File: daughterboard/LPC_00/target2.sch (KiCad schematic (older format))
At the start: 16 parts, among them U2 LPC55S69JBD64K

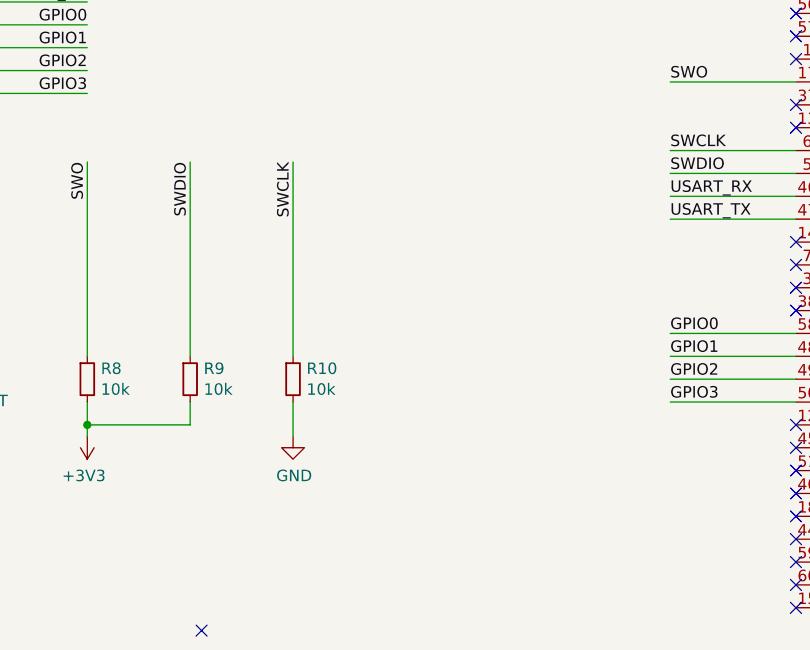
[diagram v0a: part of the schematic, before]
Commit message: ERC on daughterboards
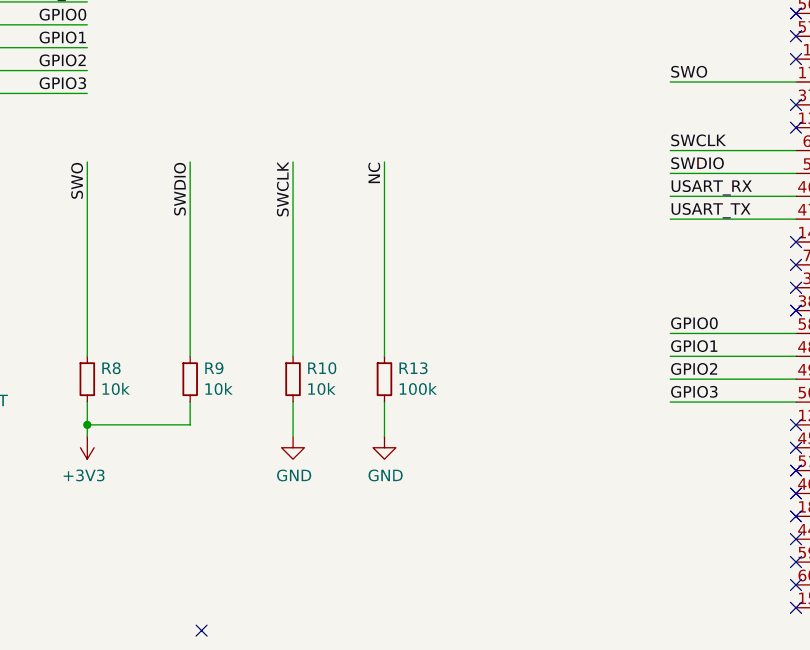
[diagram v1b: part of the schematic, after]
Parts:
- added R13: 100k, symbol Device:R_Small
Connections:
- net GND: now also R13.2
- net TDI|NC_2: now also R13.1
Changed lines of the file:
@@
 	8900 2200 8400 2200
-Wire Wire Line
-	7250 2150 7850 2150
 Wire Wire Line
 	7850 2150 7850 2500
@@
 NoConn ~ 7250 3100
 NoConn ~ 2700 5450
+Text Label 3500 3400 3    50   ~ 0
+NC
+$Comp
+L Device:R_Small R13
+U 1 1 618FD562
+P 3500 4350
+F 0 "R13" H 3559 4396 50  0000 L CNN
+F 1 "100k" H 3559 4305 50  0000 L CNN
+F 2 "" H 3500 4350 50  0001 C CNN
+F 3 "~" H 3500 4350 50  0001 C CNN
+	1    3500 4350
+	1    0    0    -1
+$EndComp
+Wire Wire Line
+	3500 4600 3500 4450
+$Comp
+L power:GND #PWR032
+U 1 1 618FD569
+P 3500 4600
+F 0 "#PWR032" H 3500 4350 50  0001 C CNN
+F 1 "GND" H 3505 4427 50  0000 C CNN
+F 2 "" H 3500 4600 50  0001 C CNN
+F 3 "" H 3500 4600 50  0001 C CNN
+	1    3500 4600
+	1    0    0    -1
+$EndComp
+Wire Wire Line
+	3500 3400 3500 4250
+Wire Wire Line
+	7250 2150 7850 2150
 $EndSCHEMATC

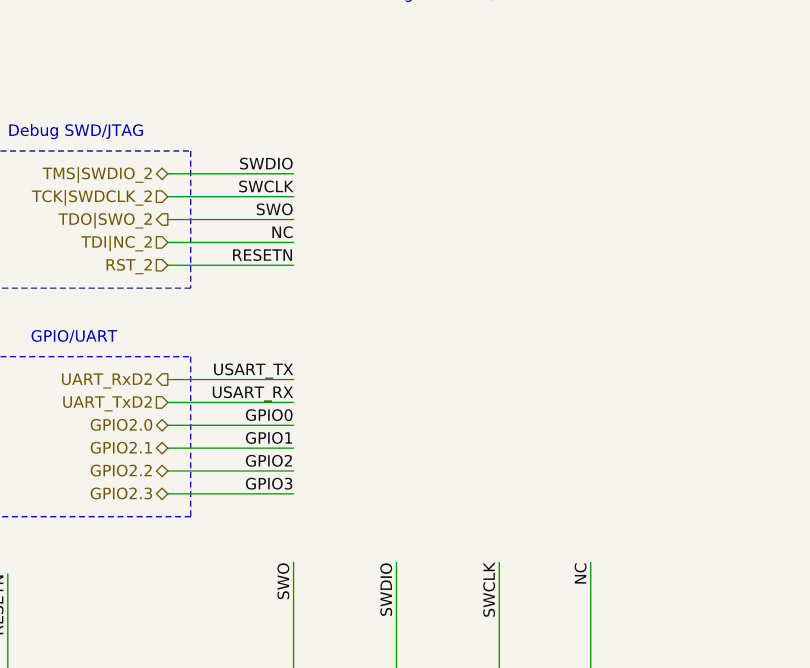
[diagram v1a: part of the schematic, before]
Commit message: added testpoints to daughterboards, updated readme
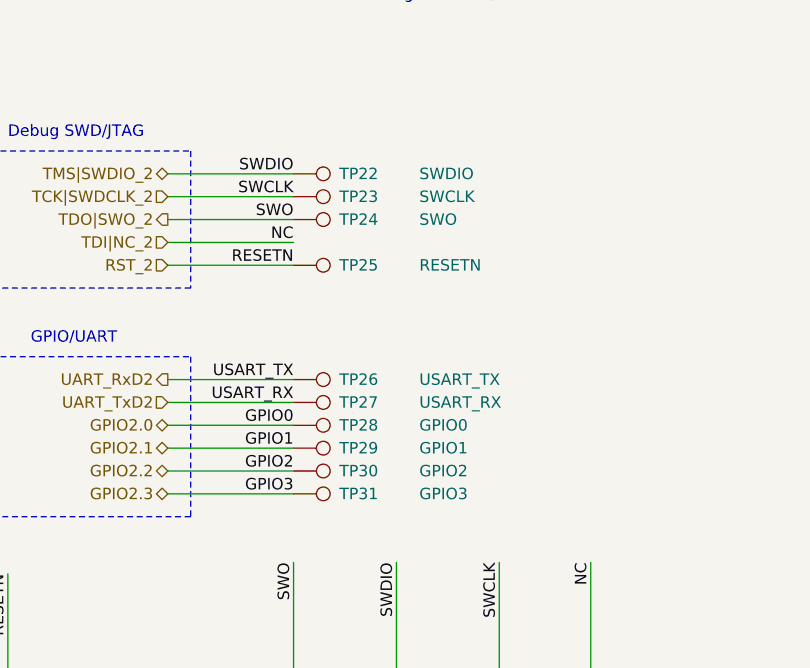
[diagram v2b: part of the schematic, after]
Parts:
- added TP22: SWDIO, symbol Connector:TestPoint
- added TP23: SWCLK, symbol Connector:TestPoint
- added TP24: SWO, symbol Connector:TestPoint
- added TP25: RESETN, symbol Connector:TestPoint
- added TP26: USART_TX, symbol Connector:TestPoint
- added TP27: USART_RX, symbol Connector:TestPoint
- added TP28: GPIO0, symbol Connector:TestPoint
- added TP29: GPIO1, symbol Connector:TestPoint
- added TP30: GPIO2, symbol Connector:TestPoint
- added TP31: GPIO3, symbol Connector:TestPoint
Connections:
- net GPIO2.0: now also TP28.1
- net GPIO2.1: now also TP29.1
- net GPIO2.2: now also TP30.1
- net GPIO2.3: now also TP31.1
- net RST_2: now also TP25.1
- net TCK|SWDCLK_2: now also TP23.1
- net TDO|SWO_2: now also TP24.1
- net TMS|SWDIO_2: now also TP22.1
- net UART_RxD2: now also TP26.1
- net UART_TxD2: now also TP27.1
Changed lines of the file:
@@
 Wire Wire Line
 	7250 2150 7850 2150
+$Comp
+L Connector:TestPoint TP22
+U 1 1 6190A42B
+P 2200 1700
+F 0 "TP22" V 2200 1900 50  0000 L CNN
+F 1 "SWDIO" V 2200 2250 50  0000 L CNN
+F 2 "" H 2400 1700 50  0001 C CNN
+F 3 "~" H 2400 1700 50  0001 C CNN
+	1    2200 1700
+	0    1    1    0
+$EndComp
+$Comp
+L Connector:TestPoint TP23
+U 1 1 6190C0EB
+P 2200 1800
+F 0 "TP23" V 2200 2000 50  0000 L CNN
+F 1 "SWCLK" V 2200 2350 50  0000 L CNN
+F 2 "" H 2400 1800 50  0001 C CNN
+F 3 "~" H 2400 1800 50  0001 C CNN
+	1    2200 1800
+	0    1    1    0
+$EndComp
+$Comp
+L Connector:TestPoint TP24
+U 1 1 6190C3D1
+P 2200 1900
+F 0 "TP24" V 2200 2100 50  0000 L CNN
+F 1 "SWO" V 2200 2450 50  0000 L CNN
+F 2 "" H 2400 1900 50  0001 C CNN
+F 3 "~" H 2400 1900 50  0001 C CNN
+	1    2200 1900
+	0    1    1    0
+$EndComp
+$Comp
+L Connector:TestPoint TP25
+U 1 1 6190C6D5
+P 2200 2100
+F 0 "TP25" V 2200 2300 50  0000 L CNN
+F 1 "RESETN" V 2200 2650 50  0000 L CNN
+F 2 "" H 2400 2100 50  0001 C CNN
+F 3 "~" H 2400 2100 50  0001 C CNN
+	1    2200 2100
+	0    1    1    0
+$EndComp
+$Comp
+L Connector:TestPoint TP26
+U 1 1 6190CD38
+P 2200 2600
+F 0 "TP26" V 2200 2800 50  0000 L CNN
+F 1 "USART_TX" V 2200 3150 50  0000 L CNN
+F 2 "" H 2400 2600 50  0001 C CNN
+F 3 "~" H 2400 2600 50  0001 C CNN
+	1    2200 2600
+	0    1    1    0
+$EndComp
+$Comp
+L Connector:TestPoint TP27
+U 1 1 6190D403
+P 2200 2700
+F 0 "TP27" V 2200 2900 50  0000 L CNN
+F 1 "USART_RX" V 2200 3250 50  0000 L CNN
+F 2 "" H 2400 2700 50  0001 C CNN
+F 3 "~" H 2400 2700 50  0001 C CNN
+	1    2200 2700
+	0    1    1    0
+$EndComp
+$Comp
+L Connector:TestPoint TP28
+U 1 1 6190D9F7
+P 2200 2800
+F 0 "TP28" V 2200 3000 50  0000 L CNN
+F 1 "GPIO0" V 2200 3350 50  0000 L CNN
+F 2 "" H 2400 2800 50  0001 C CNN
+F 3 "~" H 2400 2800 50  0001 C CNN
+	1    2200 2800
+	0    1    1    0
+$EndComp
+$Comp
+L Connector:TestPoint TP29
+U 1 1 6190DCED
+P 2200 2900
+F 0 "TP29" V 2200 3100 50  0000 L CNN
+F 1 "GPIO1" V 2200 3450 50  0000 L CNN
+F 2 "" H 2400 2900 50  0001 C CNN
+F 3 "~" H 2400 2900 50  0001 C CNN
+	1    2200 2900
+	0    1    1    0
+$EndComp
+$Comp
+L Connector:TestPoint TP30
+U 1 1 6190E02F
+P 2200 3000
+F 0 "TP30" V 2200 3200 50  0000 L CNN
+F 1 "GPIO2" V 2200 3550 50  0000 L CNN
+F 2 "" H 2400 3000 50  0001 C CNN
+F 3 "~" H 2400 3000 50  0001 C CNN
+	1    2200 3000
+	0    1    1    0
+$EndComp
+$Comp
+L Connector:TestPoint TP31
+U 1 1 6190E301
+P 2200 3100
+F 0 "TP31" V 2200 3300 50  0000 L CNN
+F 1 "GPIO3" V 2200 3650 50  0000 L CNN
+F 2 "" H 2400 3100 50  0001 C CNN
+F 3 "~" H 2400 3100 50  0001 C CNN
+	1    2200 3100
+	0    1    1    0
+$EndComp
 $EndSCHEMATC
